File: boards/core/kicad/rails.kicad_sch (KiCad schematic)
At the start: 26 parts, among them U4 SY8303AIC, U5 SY8089A1AAC, U6 LP5907-3.3

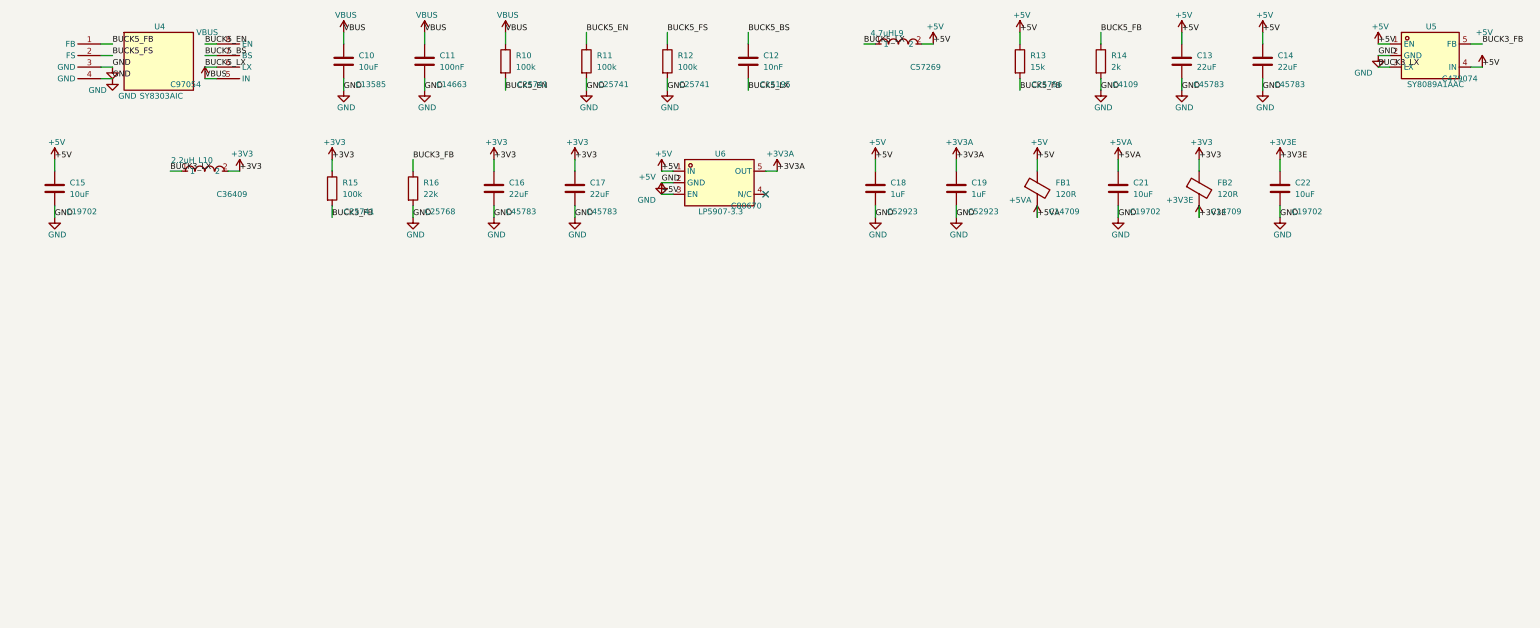
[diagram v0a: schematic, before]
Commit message: The boards will work on the first spin: independent engineering reviews of Lite and core, fixes and contingencies built…
* First-spin review: the brief each domain reviewer works from

* First-spin review: partial drafts saved before the reviewers' login d…

…ropped

* First-spin review: power, audio, digital and thermal reviews of lite-…

…main and core, with their sims

* core carries its EasyEDA CPL model cache, so its dfm gate runs withou…

…t EasyEDA (red on 403 otherwise); DFM review

* First-spin review: parts pin-to-pad audit of both boards

* Lite board after the first-spin review: amp SDZ, PVDD switch hold-off…

… and soft start, line-in headroom, 5 V loop, RCA slots, HRO USB-C and CH340B, speaker loopback taps; regenerated on hwde c23e27e, all gates pass

Review-2 findings fixed on lite-main as an ECO on the routed board (no
re-route): AUDIO-4/DIGITAL-14, POWER-3/4/10, AUDIO-7, DFM-2, stock swaps.
Also: the speaker loopback taps (task 261029-033806) and the hwde refresh
(task 261029-004401) for this board. Known-unknowns list and its order-step
check (tools/known_unknowns.py). Unit cost at 100: 13.16 (was 13.05).

* core (Plus/Ultra) after the first-spin review: TCA9539 with ESP32 res…

…et, 5 A path via patches and through-hole USB4085, antenna keep-out, PVDD switch SOA and PD-PG gating, OPA1678 headroom, RCA and TOSLINK holes, front IR, 49.152 MHz DAC clock, speaker loopback taps; all gates pass

Review-2 blockers fixed on core: DIGITAL-1/2/PARTS-4, POWER-1, DFM-1, PARTS-7;
THERMAL-1 handled by a lid-pressed heatsink plus firmware governor (no room
for clip holes). Majors: POWER-2/6, AUDIO-1/2/3, DIGITAL-19, DFM-4. Done as an
ECO on the routed board; Ultra zone-B taps left out (no control line).

* First-spin review: every finding's disposition, known-unknowns resolv…

…ed for Lite and Plus (order gate by tier), firmware duties for core, R45 2.2k, honest TPA3221 thermal constraint, Plus/Ultra cost estimate

* Heatsink options for the TPA3221 checked aga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
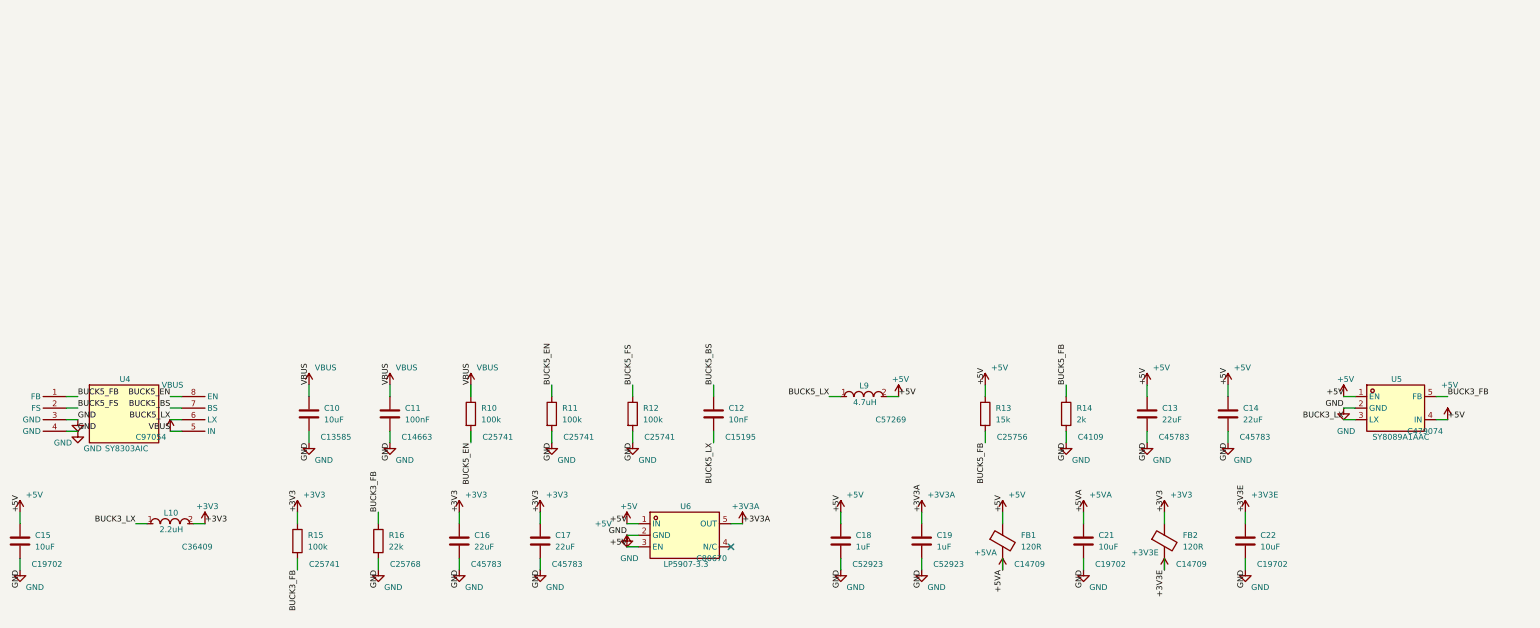
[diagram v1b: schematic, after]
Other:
- moved on the sheet: C10, C11, C12, C13, C14, C15, C16, C17, C18, C19, C21, C22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
